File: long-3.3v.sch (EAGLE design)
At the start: 22 parts, among them U1 USD-SOCKET, U2 MCP73831, U4 ADXL375BCCZ, X1 Micro USB

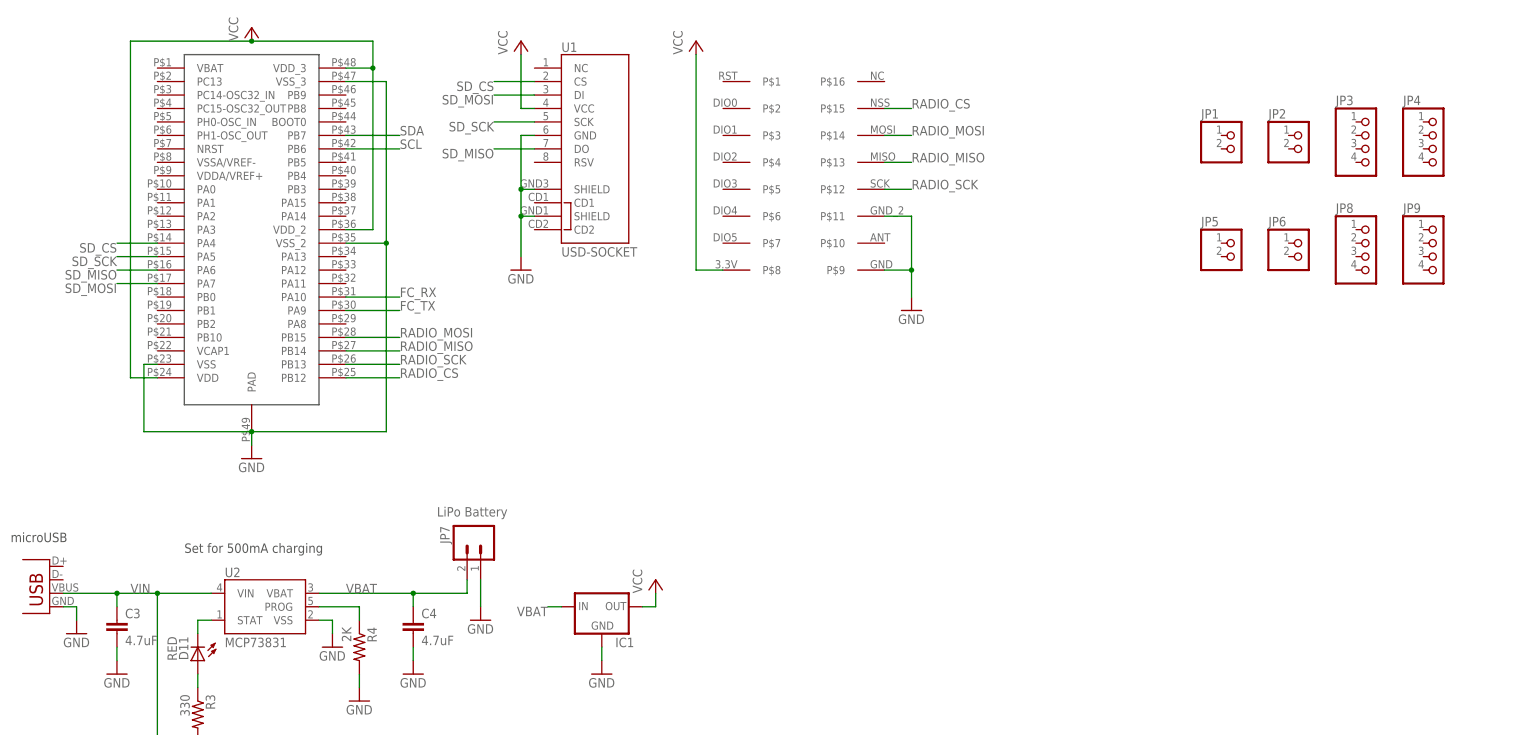
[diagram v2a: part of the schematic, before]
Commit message: Connected USB & Crystal Routed base PCB
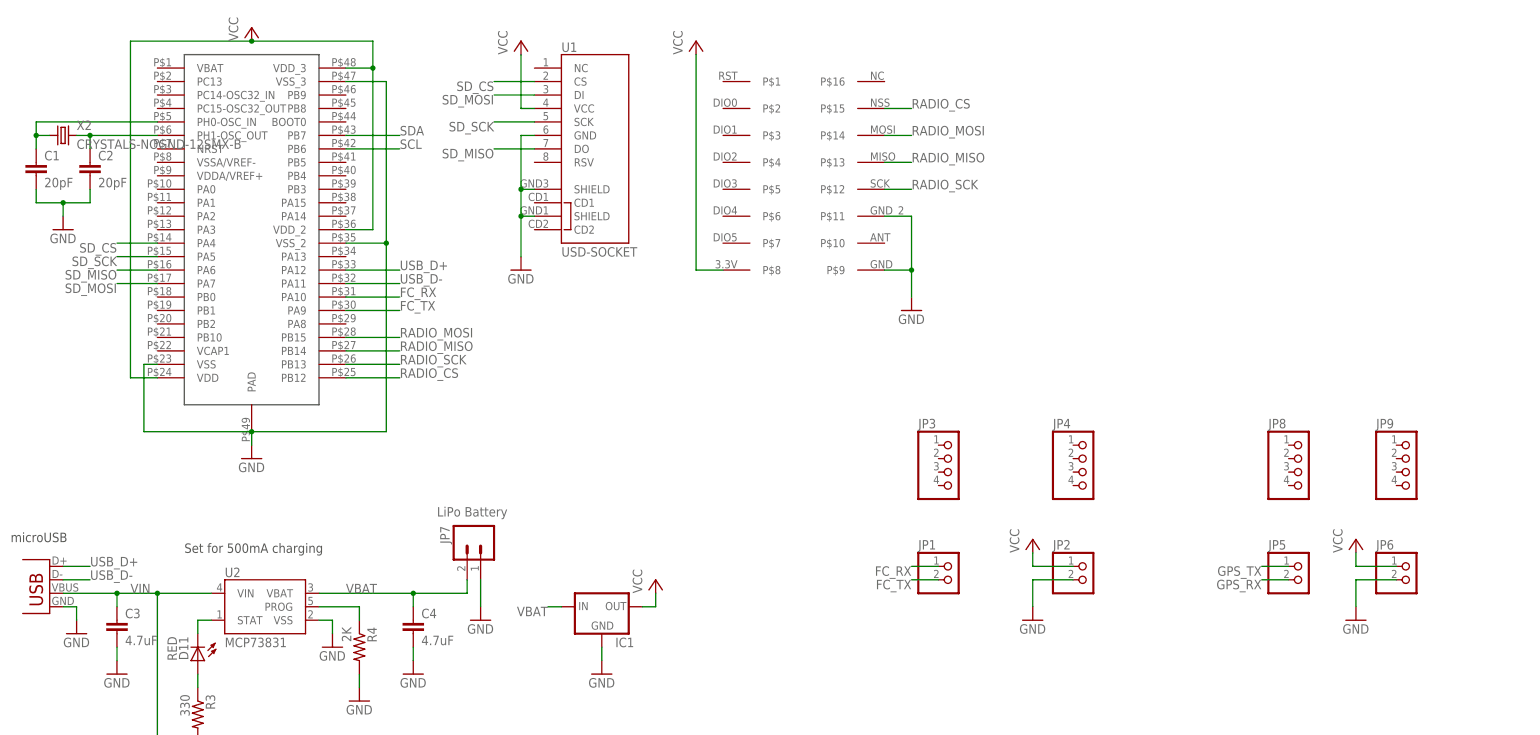
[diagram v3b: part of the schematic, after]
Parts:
- added C1, C2: 20pF, rcl:C-EUC0402
- added X2: CRYSTALS-NOGND-12SMX-B, IQD-Frequency-Products:CRYSTALS-NOGND-12SMX-B
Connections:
- new net N$1: C1.1, U$1.PH0-OSC_IN, X2.1
- new net N$2: C2.1, U$1.PH1-OSC_OUT, X2.2
- new net USB_D+: U$1.PA12, X1.D+
- new net USB_D-: U$1.PA11, X1.D-
- net FC_RX: now also JP1.1
- net FC_TX: now also JP1.2
- net GND: now also C1.2, C2.2, JP2.2, JP6.2
- net GPS_RX: now also JP5.2
- net GPS_TX: now also JP5.1
- net VCC: now also JP2.1, JP6.1
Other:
- moved on the sheet: JP1, JP2, JP3, JP4, JP5, JP6, JP8, JP9
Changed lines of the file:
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@@
 <part name="GND6" library="supply1" deviceset="GND" device=""/>
 <part name="GND8" library="supply1" deviceset="GND" device=""/>
+<part name="X2" library="IQD-Frequency-Products" deviceset="CRYSTALS-NOGND" device="-12SMX-B">
+<attribute name="OC_FARNELL" value="1276690"/>
+</part>
+<part name="C1" library="rcl" deviceset="C-EU" device="C0402" value="20pF"/>
+<part name="C2" library="rcl" deviceset="C-EU" device="C0402" value="20pF"/>
+<part name="GND9" library="supply1" deviceset="GND" device=""/>
+<part name="P+8" library="supply1" deviceset="VCC" device=""/>
+<part name="GND10" library="supply1" deviceset="GND" device=""/>
+<part name="P+9" library="supply1" deviceset="VCC" device=""/>
+<part name="GND11" library="supply1" deviceset="GND" device=""/>
 </parts>
 <sheets>
@@
 <instance part="X1" gate="G$1" x="15.24" y="38.1" rot="MR0"/>
 <instance part="U$2" gate="G$1" x="335.28" y="55.88"/>
-<instance part="JP1" gate="G$1" x="238.76" y="124.46"/>
-<instance part="JP2" gate="G$1" x="251.46" y="124.46"/>
-<instance part="JP3" gate="A" x="264.16" y="124.46"/>
-<instance part="JP4" gate="A" x="276.86" y="124.46"/>
-<instance part="JP5" gate="G$1" x="238.76" y="104.14"/>
-<instance part="JP6" gate="G$1" x="251.46" y="104.14"/>
-<instance part="JP8" gate="A" x="264.16" y="104.14"/>
-<instance part="JP9" gate="A" x="276.86" y="104.14"/>
+<instance part="JP1" gate="G$1" x="185.42" y="43.18"/>
+<instance part="JP2" gate="G$1" x="210.82" y="43.18"/>
+<instance part="JP3" gate="A" x="185.42" y="63.5"/>
+<instance part="JP4" gate="A" x="210.82" y="63.5"/>
+<instance part="JP5" gate="G$1" x="251.46" y="43.18"/>
+<instance part="JP6" gate="G$1" x="271.78" y="43.18"/>
+<instance part="JP8" gate="A" x="251.46" y="63.5"/>
+<instance part="JP9" gate="A" x="271.78" y="63.5"/>
 <instance part="U4" gate="A" x="312.42" y="127"/>
 <instance part="U$1" gate="G$1" x="55.88" y="119.38"/>
@@
 <instance part="GND6" gate="1" x="360.68" y="22.86"/>
 <instance part="GND8" gate="1" x="408.94" y="93.98"/>
+<instance part="X2" gate="G$1" x="17.78" y="127">
+<attribute name="OC_FARNELL" x="17.78" y="127" size="1.778" layer="96" display="off"/>
+</instance>
+<instance part="C1" gate="G$1" x="12.7" y="121.92"/>
+<instance part="C2" gate="G$1" x="22.86" y="121.92"/>
+<instance part="GND9" gate="1" x="17.78" y="109.22"/>
+<instance part="P+8" gate="VCC" x="200.66" y="50.8"/>
+<instance part="GND10" gate="1" x="200.66" y="35.56"/>
+<instance part="P+9" gate="VCC" x="261.62" y="50.8"/>
+<instance part="GND11" gate="1" x="261.62" y="35.56"/>
 </instances>
 <busses>
@@
 <pinref part="GND8" gate="1" pin="GND"/>
 </segment>
+<segment>
+<pinref part="C2" gate="G$1" pin="2"/>
+<wire x1="22.86" y1="116.84" x2="22.86" y2="114.3" width="0.1524" layer="91"/>
+<wire x1="22.86" y1="114.3" x2="17.78" y2="114.3" width="0.1524" layer="91"/>
+<pinref part="C1" gate="G$1" pin="2"/>
+<wire x1="17.78" y1="114.3" x2="12.7" y2="114.3" width="0.1524" layer="91"/>
+<wire x1="12.7" y1="114.3" x2="12.7" y2="116.84" width="0.1524" layer="91"/>
+<wire x1="17.78" y1="114.3" x2="17.78" y2="111.76" width="0.1524" layer="91"/>
+<junction x="17.78" y="114.3"/>
+<pinref part="GND9" gate="1" pin="GND"/>
+</segment>
+<segment>
+<pinref part="GND10" gate="1" pin="GND"/>
+<wire x1="200.66" y1="43.18" x2="200.66" y2="38.1" width="0.1524" layer="91"/>
+<pinref part="JP2" gate="G$1" pin="2"/>
+<wire x1="208.28" y1="43.18" x2="200.66" y2="43.18" width="0.1524" layer="91"/>
+</segment>
+<segment>
+<pinref part="GND11" gate="1" pin="GND"/>
+<wire x1="261.62" y1="43.18" x2="261.62" y2="38.1" width="0.1524" layer="91"/>
+<pinref part="JP6" gate="G$1" pin="2"/>
+<wire x1="269.24" y1="43.18" x2="261.62" y2="43.18" width="0.1524" layer="91"/>
+</segment>
 </net>
 <net name="VBAT" class="0">
@@
 <pinref part="P+7" gate="VCC" pin="VCC"/>
 </segment>
+<segment>
+<pinref part="P+8" gate="VCC" pin="VCC"/>
+<wire x1="200.66" y1="45.72" x2="200.66" y2="48.26" width="0.1524" layer="91"/>
+<pinref part="JP2" gate="G$1" pin="1"/>
+<wire x1="200.66" y1="45.72" x2="208.28" y2="45.72" width="0.1524" layer="91"/>
+</segment>
+<segment>
+<pinref part="P+9" gate="VCC" pin="VCC"/>
+<wire x1="261.62" y1="45.72" x2="261.62" y2="48.26" width="0.1524" layer="91"/>
+<pinref part="JP6" gate="G$1" pin="1"/>
+<wire x1="261.62" y1="45.72" x2="269.24" y2="45.72" width="0.1524" layer="91"/>
+</segment>
 </net>
 <net name="SD_MISO" class="0">
@@
 <label x="363.22" y="40.64" size="1.778" layer="95"/>
 </segment>
+<segment>
+<pinref part="JP5" gate="G$1" pin="2"/>
+<wire x1="248.92" y1="43.18" x2="243.84" y2="43.18" width="0.1524" layer="91"/>
+<label x="243.84" y="43.18" size="1.778" layer="95" rot="R180"/>
+</segment>
 </net>
 <net name="GPS_TX" class="0">
@@
 <label x="363.22" y="35.56" size="1.778" layer="95"/>
 </segment>
+<segment>
+<pinref part="JP5" gate="G$1" pin="1"/>
+<wire x1="248.92" y1="45.72" x2="243.84" y2="45.72" width="0.1524" layer="91"/>
+<label x="243.84" y="45.72" size="1.778" layer="95" rot="R180"/>
+</segment>
 </net>
 <net name="SCL" class="0">
@@
 <label x="81.28" y="93.98" size="1.778" layer="95"/>
 </segment>
+<segment>
+<pinref part="JP1" gate="G$1" pin="2"/>
+<wire x1="182.88" y1="43.18" x2="177.8" y2="43.18" width="0.1524" layer="91"/>
+<label x="177.8" y="43.18" size="1.778" layer="95" rot="R180"/>
+</segment>
 </net>
 <net name="FC_RX" class="0">
@@
 <label x="81.28" y="96.52" size="1.778" layer="95"/>
 </segment>
-</net>
+<segment>
+<pinref part="JP1" gate="G$1" pin="1"/>
+<wire x1="182.88" y1="45.72" x2="177.8" y2="45.72" width="0.1524" layer="91"/>
+<label x="177.8" y="45.72" size="1.778" layer="95" rot="R180"/>
+</segment>
+</net>
+<net name="N$1" class="0">
+<segment>
+<pinref part="U$1" gate="G$1" pin="PH0-OSC_IN"/>
+<wire x1="35.56" y1="129.54" x2="12.7" y2="129.54" width="0.1524" layer="91"/>
+<pinref part="C1" gate="G$1" pin="1"/>
+<wire x1="12.7" y1="129.54" x2="12.7" y2="127" width="0.1524" layer="91"/>
+<pinref part="X2" gate="G$1" pin="1"/>
+<wire x1="12.7" y1="127" x2="12.7" y2="124.46" width="0.1524" layer="91"/>
+<wire x1="15.24" y1="127" x2="12.7" y2="127" width="0.1524" layer="91"/>
+<junction x="12.7" y="127"/>
+</segment>
+</net>
+<net name="N$2" class="0">
+<segment>
+<pinref part="C2" gate="G$1" pin="1"/>
+<wire x1="22.86" y1="127" x2="22.86" y2="124.46" width="0.1524" layer="91"/>
+<pinref part="U$1" gate="G$1" pin="PH1-OSC_OUT"/>
+<wire x1="22.86" y1="127" x2="35.56" y2="127" width="0.1524" layer="91"/>
+<pinref part="X2" gate="G$1" pin="2"/>
+<wire x1="22.86" y1="127" x2="20.32" y2="127" width="0.1524" layer="91"/>
+<junction x="22.86" y="127"/>
+</segment>
+</net>
+<net name="USB_D-" class="0">
+<segment>
+<pinref part="U$1" gate="G$1" pin="PA11"/>
+<wire x1="71.12" y1="99.06" x2="81.28" y2="99.06" width="0.1524" layer="91"/>
+<label x="81.28" y="99.06" size="1.778" layer="95"/>
+</segment>
+<segment>
+<pinref part="X1" gate="G$1" pin="D-"/>
+<wire x1="17.78" y1="43.18" x2="22.86" y2="43.18" width="0.1524" layer="91"/>
+<label x="22.86" y="43.18" size="1.778" layer="95"/>
+</segment>
+</net>
+<net name="USB_D+" class="0">
+<segment>
+<pinref part="U$1" gate="G$1" pin="PA12"/>
+<wire x1="71.12" y1="101.6" x2="81.28" y2="101.6" width="0.1524" layer="91"/>
+<label x="81.28" y="101.6" size="1.778" layer="95"/>
+</segment>
+<segment>
+<pinref part="X1" gate="G$1" pin="D+"/>
+<wire x1="17.78" y1="45.72" x2="22.86" y2="45.72" width="0.1524" layer="91"/>
+<label x="22.86" y="45.72" size="1.778" layer="95"/>
+</segment>
+</net>

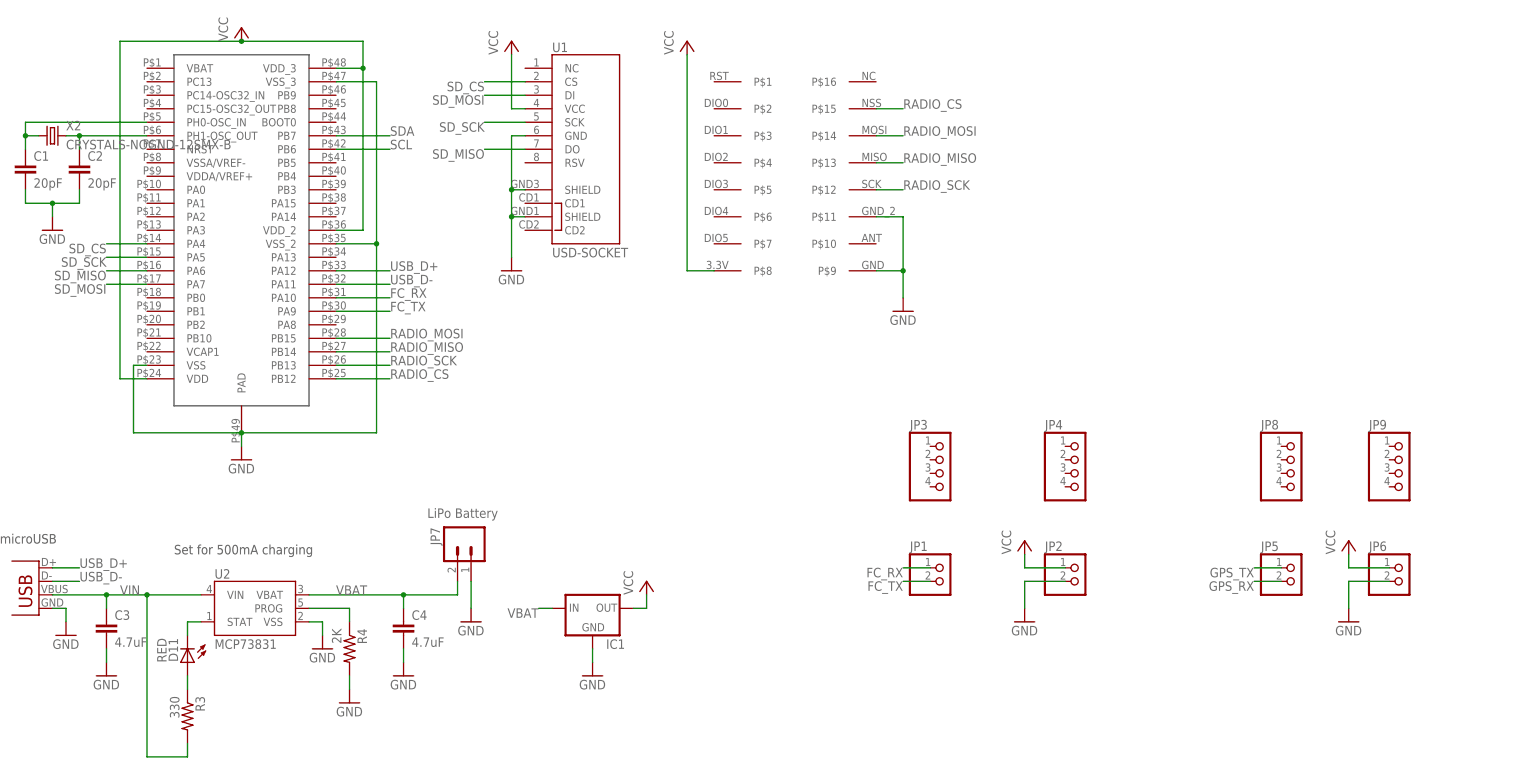
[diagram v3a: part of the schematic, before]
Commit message: Added Components Added decoupling capacitors Changed pin headers to round pads
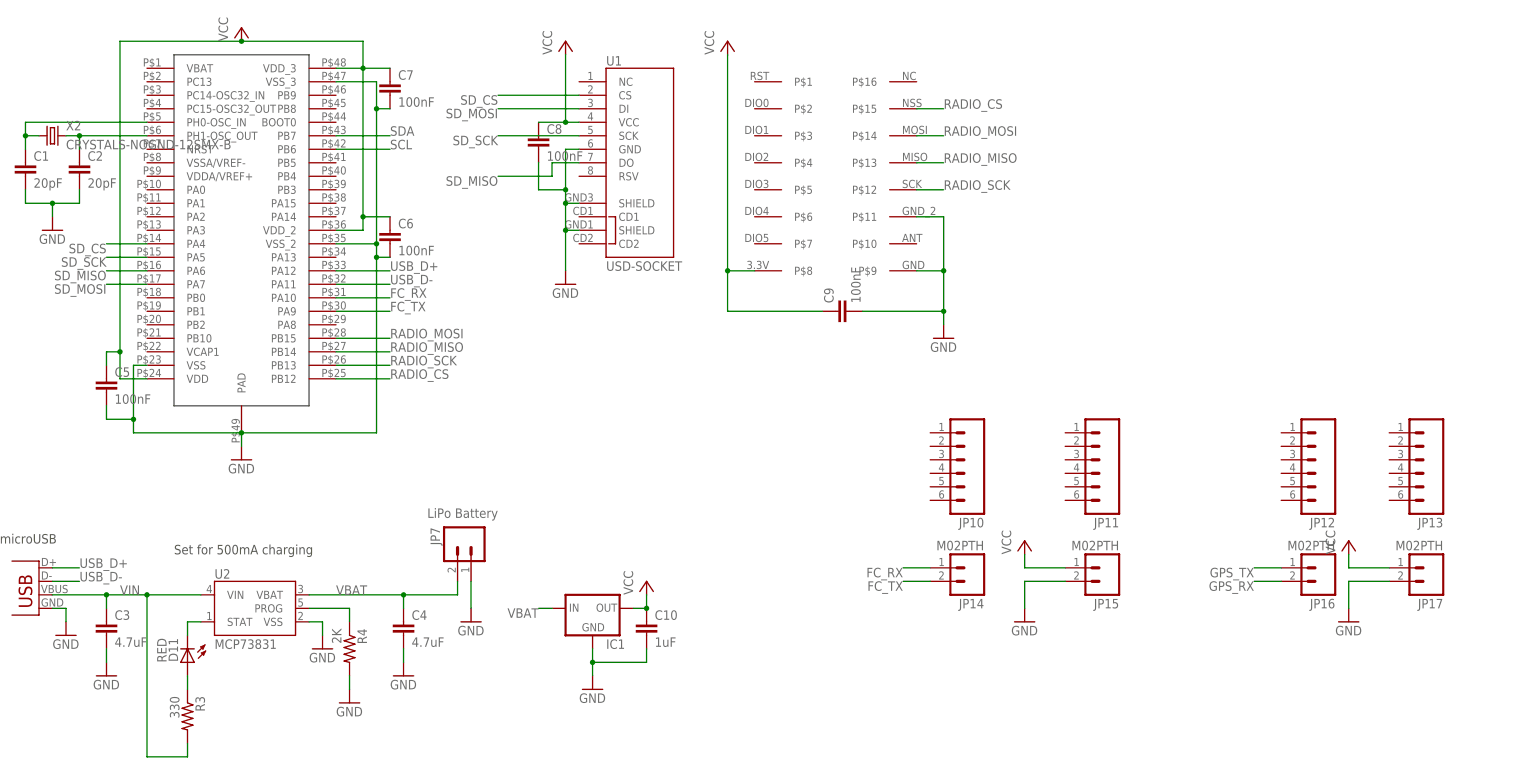
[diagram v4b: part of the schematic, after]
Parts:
- removed JP1, JP2, JP5, JP6: (no value), pinhead:PINHD-1X2
- removed JP3, JP4, JP8, JP9: (no value), pinhead:PINHD-1X4
- added C10: 1uF, rcl:C-EUC0402
- added C5, C6, C7, C8, C9: 100nF, rcl:C-EUC0402
- added JP10, JP11, JP12, JP13: (no value), SparkFun-Connectors:M06SIP
- added JP14, JP15, JP16, JP17: M02PTH, SparkFun-Connectors:M02PTH
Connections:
- net FC_RX: now also JP14.1; no longer JP1.1
- net FC_TX: now also JP14.2; no longer JP1.2
- net GND: now also C10.2, C5.2, C6.2, C7.2, C8.2, C9.2, JP15.2, JP17.2; no longer JP2.2, JP6.2
- net GPS_RX: now also JP16.2; no longer JP5.2
- net GPS_TX: now also JP16.1; no longer JP5.1
- net VCC: now also C10.1, C5.1, C6.1, C7.1, C8.1, C9.1, JP15.1, JP17.1; no longer JP2.1, JP6.1
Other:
- moved on the sheet: U1
